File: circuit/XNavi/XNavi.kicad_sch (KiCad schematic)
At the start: 0 parts

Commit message: initial commit
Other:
- title: Template -> XNavi
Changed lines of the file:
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@@
 	(paper "A4")
 	(title_block
-		(title "Template")
+		(title "XNavi")
 		(rev "0.0")
 		(company "AIOLIA")

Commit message: 回路図&PCBを追加
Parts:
- added C10, C11, C12, C13, C14, C15, C2, C8, C9: 0.1u, Capacitor_SMD:C_0603_1608Metric_Pad1.08x0.95mm_HandSolder, symbol Device:C
- added C3: 1.0u, Capacitor_SMD:C_0603_1608Metric_Pad1.08x0.95mm_HandSolder, symbol Device:C
- added C4, C5: 2.2p, Capacitor_SMD:C_0603_1608Metric_Pad1.08x0.95mm_HandSolder, symbol Device:C
- added C6, C7: 2.2u, Capacitor_SMD:C_0603_1608Metric_Pad1.08x0.95mm_HandSolder, symbol Device:C
- added D3: LED, LED_SMD:LED_0603_1608Metric_Pad1.05x0.95mm_HandSolder, symbol Device:LED
- added D4, D5: LED, Diode_SMD:D_0603_1608Metric_Pad1.05x0.95mm_HandSolder, symbol Device:LED
- added J3: Micro_SD_Card_Det_Hirose_DM3AT, Connector_Card:microSD_HC_Hirose_DM3D-SF, symbol Connector:Micro_SD_Card_Det_Hirose_DM3AT
- added J4: Conn_01x02, Connector_JST:JST_PH_B2B-PH-SM4-TB_1x02-1MP_P2.00mm_Vertical, symbol Connector_Generic:Conn_01x02
- added J5: Conn_ST_STDC14, AIOLIA:CONN14_3220-14_CNC, symbol Connector:Conn_ST_STDC14
- added J6: Conn_01x04, Connector_JST:JST_PH_S4B-PH-SM4-TB_1x04-1MP_P2.00mm_Horizontal, symbol Connector_Generic:Conn_01x04
- added J7: Conn_02x03_Odd_Even, Connector_PinHeader_2.54mm:PinHeader_2x03_P2.54mm_Vertical, symbol Connector_Generic:Conn_02x03_Odd_Even
- added J9: Conn_Coaxial, Connector_Coaxial:U.FL_Molex_MCRF_73412-0110_Vertical, symbol Connector:Conn_Coaxial
- added JP1: Jumper_2_Open, Jumper:SolderJumper-2_P1.3mm_Open_RoundedPad1.0x1.5mm, symbol Jumper:Jumper_2_Open
- added L1: 27n, Inductor_SMD:L_0805_2012Metric_Pad1.15x1.40mm_HandSolder, symbol Device:L
- added R1, R11, R12, R2, R3, R4, R5, R6: 10k, Resistor_SMD:R_0603_1608Metric_Pad0.98x0.95mm_HandSolder, symbol Device:R
- added R10: 10k (DNP), Resistor_SMD:R_0603_1608Metric_Pad0.98x0.95mm_HandSolder, symbol Device:R
- added R13: 120, Resistor_SMD:R_0603_1608Metric_Pad0.98x0.95mm_HandSolder, symbol Device:R
- added R14: 10, Resistor_SMD:R_0603_1608Metric_Pad0.98x0.95mm_HandSolder, symbol Device:R
- added R15, R16, R17: 200, Resistor_SMD:R_0603_1608Metric_Pad0.98x0.95mm_HandSolder, symbol Device:R
- added SW1: SW_Slide, AIOLIA:SW_Slide, symbol AIOLIA:SW_Slide
- added SW2: SW_Push, Button_Switch_SMD:SW_Push_1P1T_NO_6x6mm_H9.5mm, symbol Switch:SW_Push
- added U2: ~, AIOLIA:SOT95P280X130-5N, symbol AIOLIA:NJM2866F33
- added U3: STM32H573RITx, Package_QFP:LQFP-64_10x10mm_P0.5mm, symbol MCU_ST_STM32H5:STM32H573RITx
- added U4: ~, Package_TO_SOT_SMD:SOT-23-8_Handsoldering, symbol AIOLIA:TCAN3413DDR
- added U5: ASM330LHHTR, Package_LGA:LGA-14_3x2.5mm_P0.5mm_LayoutBorder3x4y, symbol AIOLIA:ASM330LHHTR
- added U6: MAX-M10S, RF_GPS:ublox_MAX, symbol RF_GPS:MAX-M10S
- added Y1: 16MHz, Crystal:Crystal_HC52-U_Vertical, symbol Device:Crystal
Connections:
- new net: C6.1, U3.30 (VCAP)
- new net: C4.2, U3.5 (PH0), Y1.1
- new net: C5.2, U3.6 (PH1), Y1.2
- new net: C7.1, U3.62 (VCAP)
- new net: J4.1 (Pin_1), SW1.2 (B), SW1.5 (B)
- new net: D4.2 (A), R16.2
- new net: J6.2 (Pin_2), R13.1, U4.6 (CANL)
- new net: J6.1 (Pin_1), R13.2, U4.7 (CANH)
- new net: D5.2 (A), R17.2
- new net: D3.2 (A), R15.2
- new net: L1.2, R14.1
- new net: R14.2, U6.14 (VCC_RF)
- new net: J6.4 (Pin_4), JP1.1 (A)
- new net +3V3: C10.1, C11.1, C12.1, C13.1, C14.1, C15.1, C3.2, C8.1, C9.1, J3.4 (VDD), J5.3 (VCC), J7.1 (Pin_1), J7.2 (Pin_2), R1.2, R10.2, R12.1, R2.2, R3.2, R4.2, R5.2, R6.2, U2.5 (Vout), U3.1 (VBAT), U3.13 (VDDA), U3.19 (VDD), U3.32 (VDD), U3.48 (VDD), U3.64 (VDD), U4.3 (VCC), U4.5 (VIO), U5.5 (VDD_IO), U5.8 (VDD), U6.6 (V_BCKP), U6.7 (VCC_IO), U6.8 (VCC)
- new net AIN0: J7.6 (Pin_6), U3.8 (PC0)
- new net AIN1: J7.5 (Pin_5), U3.9 (PC1)
- new net AIN2: U3.10 (PC2)
- new net AIN3: U3.11 (PC3)
- new net BOOT: R10.1, R11.1, U3.60 (BOOT0)
- new net FDCAN2_RX: U3.33 (PB12), U4.4 (RXD)
- new net FDCAN2_TX: U3.34 (PB13), U4.1 (TXD)
- new net GND: C10.2, C11.2, C12.2, C13.2, C14.2, C15.2, C2.2, C3.1, C4.1, C5.1, C6.2, C7.2, C8.2, C9.2, D3.1 (K), D4.1 (K), D5.1 (K), J3.11 (SHIELD), J3.6 (VSS), J3.9 (DET_B), J4.2 (Pin_2), J5.11 (GNDDetect), J5.5 (GND), J5.7 (GND), J6.3 (Pin_3), J7.3 (Pin_3), J7.4 (Pin_4), J9.2 (Ext), R11.2, SW2.2, U2.2 (GND), U3.12 (VSSA), U3.18 (VSS), U3.31 (VSS), U3.47 (VSS), U3.63 (VSS), U4.2 (GND), U4.8 (STB), U5.2 (RES), U5.3 (RES), U5.6 (GND), U5.7 (GND), U6.1 (GND), U6.10 (GND), U6.12 (GND)
- new net I2C1_SCL: U3.58 (PB6)
- new net I2C1_SDA: U3.59 (PB7)
- new net LED0: R16.1, U3.24 (PC4)
- new net LED1: R17.1, U3.25 (PC5)
- new net LED2: U3.3 (PC14)
- new net LED3: U3.4 (PC15)
- new net PPS: R15.1, U3.41 (PA8), U6.4 (TIMEPULSE)
- new net RF: J9.1 (In), L1.1, U6.11 (RF_IN)
- new net RST: R12.2, SW2.1, U3.7 (NRST)
- new net RX1: J5.13 (VCP_RX), U3.43 (PA10)
- new net RX2: U3.17 (PA3)
- new net RX6: U3.38 (PC7), U6.3 (RXD)
- new net SDIO_CLK: J3.5 (CLK), U3.53 (PC12)
- new net SDIO_CMD: J3.3 (CMD), R3.1, U3.54 (PD2)
- new net SDIO_DAT0: J3.7 (DAT0), R4.1, U3.39 (PC8)
- new net SDIO_DAT1: J3.8 (DAT1), R5.1, U3.40 (PC9)
- new net SDIO_DAT2: J3.1 (DAT2), R1.1, U3.51 (PC10)
- new net SDIO_DAT3: J3.2 (DAT3/CD), R2.1, U3.52 (PC11)
- new net SD_DET: J3.10 (DET_A), R6.1, U3.50 (PA15(JTDI))
- new net SPI1_CS: U3.20 (PA4), U5.12 (CS)
- new net SPI1_MISO: U3.22 (PA6), U5.1 (SDO/SA0)
- new net SPI1_MOSI: U3.23 (PA7), U5.14 (SDA)
- new net SPI1_SCK: U3.21 (PA5), U5.13 (SCL)
- new net SW: U3.2 (PC13)
- new net SWCLK: J5.6 (JCLK/SWCLK), U3.49 (PA14(JTCK)
- new net SWDIO: J5.4 (JTMS/SWDIO), U3.46 (PA13(JTMS)
- new net TX1: J5.14 (VCP_TX), U3.42 (PA9)
- new net TX2: U3.16 (PA2)
- new net TX6: U3.37 (PC6), U6.2 (TXD)
- new net VCC: C2.1, JP1.2 (B), SW1.1 (A), SW1.6 (C), U2.1 (Vin), U2.3 (CONTROL)
- no-connect marks 0 -> 29
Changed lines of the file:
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@@
 	(generator "eeschema")
 	(generator_version "8.0")
-	(paper "A4")
+	(paper "A3")
 	(title_block
 		(title "XNavi")
@@
 		(company "AIOLIA")
 	)
-	(sheet_instances
-		(path "/"
-			(page "1")
-		)
-	)
-)

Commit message: MCUをRaspberry Pi Pico(2)に変更
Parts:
- removed C10, C11, C12, C13, C8, C9: 0.1u, Capacitor_SMD:C_0603_1608Metric_Pad1.08x0.95mm_HandSolder, symbol Device:C
- removed C5: 2.2p, Capacitor_SMD:C_0603_1608Metric_Pad1.08x0.95mm_HandSolder, symbol Device:C
- removed C6, C7: 2.2u, Capacitor_SMD:C_0603_1608Metric_Pad1.08x0.95mm_HandSolder, symbol Device:C
- removed J3: Micro_SD_Card_Det_Hirose_DM3AT, Connector_Card:microSD_HC_Hirose_DM3D-SF, symbol Connector:Micro_SD_Card_Det_Hirose_DM3AT
- removed J4: Conn_01x02, Connector_JST:JST_PH_B2B-PH-SM4-TB_1x02-1MP_P2.00mm_Vertical, symbol Connector_Generic:Conn_01x02
- removed J5: Conn_ST_STDC14, AIOLIA:CONN14_3220-14_CNC, symbol Connector:Conn_ST_STDC14
- removed J6: Conn_01x04, Connector_JST:JST_PH_S4B-PH-SM4-TB_1x04-1MP_P2.00mm_Horizontal, symbol Connector_Generic:Conn_01x04
- removed J7: Conn_02x03_Odd_Even, Connector_PinHeader_2.54mm:PinHeader_2x03_P2.54mm_Vertical, symbol Connector_Generic:Conn_02x03_Odd_Even
- removed JP1: Jumper_2_Open, Jumper:SolderJumper-2_P1.3mm_Open_RoundedPad1.0x1.5mm, symbol Jumper:Jumper_2_Open
- removed R10: 10k (DNP), Resistor_SMD:R_0603_1608Metric_Pad0.98x0.95mm_HandSolder, symbol Device:R
- removed R11, R12, R4, R5, R6: 10k, Resistor_SMD:R_0603_1608Metric_Pad0.98x0.95mm_HandSolder, symbol Device:R
- removed R13: 120, Resistor_SMD:R_0603_1608Metric_Pad0.98x0.95mm_HandSolder, symbol Device:R
- removed SW1: SW_Slide, AIOLIA:SW_Slide, symbol AIOLIA:SW_Slide
- removed SW2: SW_Push, Button_Switch_SMD:SW_Push_1P1T_NO_6x6mm_H9.5mm, symbol Switch:SW_Push
- removed U2: ~, AIOLIA:SOT95P280X130-5N, symbol AIOLIA:NJM2866F33
- removed U3: STM32H573RITx, Package_QFP:LQFP-64_10x10mm_P0.5mm, symbol MCU_ST_STM32H5:STM32H573RITx
- removed U4: ~, Package_TO_SOT_SMD:SOT-23-8_Handsoldering, symbol AIOLIA:TCAN3413DDR
- removed Y1: 16MHz, Crystal:Crystal_HC52-U_Vertical, symbol Device:Crystal
- added A1: RaspberryPi_Pico, Module:RaspberryPi_Pico_SMD_HandSolder, symbol MCU_Module:RaspberryPi_Pico_Debug
- added C1: 0.1u, Capacitor_SMD:C_0603_1608Metric_Pad1.08x0.95mm_HandSolder, symbol Device:C
- added D4: LED, Diode_SMD:D_0603_1608Metric_Pad1.05x0.95mm_HandSolder, symbol Device:LED
- added J1: Micro_SD_Card_Det, Connector_Card:microSD_HC_Hirose_DM3AT-SF-PEJM5, symbol Connector:Micro_SD_Card_Det
- added J2, J4: Conn_01x06, Connector_JST:JST_ZH_B6B-ZR_1x06_P1.50mm_Vertical, symbol Connector_Generic:Conn_01x06
- added J3: Conn_01x04, Connector_JST:JST_PH_S4B-PH-K_1x04_P2.00mm_Horizontal, symbol Connector_Generic:Conn_01x04
- added J5: Conn_01x02, Connector_JST:JST_PH_S2B-PH-SM4-TB_1x02-1MP_P2.00mm_Horizontal, symbol Connector_Generic:Conn_01x02
- added R8: 200, Resistor_SMD:R_0603_1608Metric_Pad0.98x0.95mm_HandSolder, symbol Device:R
- added U1: STM32G441KBTx, Package_QFP:LQFP-32_7x7mm_P0.8mm, symbol MCU_ST_STM32G4:STM32G441KBTx
- added U2: ~, Package_TO_SOT_SMD:SOT-23-8_Handsoldering, symbol AIOLIA:TCAN3413DDR
- C3: value 1.0u -> 0.1u
- C4: value 2.2p -> 0.1u
- R1, R2: value 10k -> 100
- R3: value 10k -> 120
- renumbered C14 to C5, C15 to C6, D3 to D1, D4 to D2, D5 to D3, J9 to J6, R14 to R4, R15 to R5, R16 to R6, R17 to R7, U5 to U3, U6 to U4
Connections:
- net RX6 is gone; now on net RX1: U4.3 (RXD)
- net SDIO_DAT3 is gone; now on net GND: R2.1
- net TX6 is gone; now on net TX1: U4.2 (TXD)
- net +3V3: now also C2.1, C3.1, C4.2, A1.36 (3V3), C1.1, J1.4 (VDD), U1.1 (VDD), U1.15 (VDDA), U1.17 (VDD), U2.3 (VCC), U2.5 (VIO); no longer C3.2, R2.2, R3.2
- net GND: now also C3.2, A1.13 (GND), A1.18 (GND), A1.23 (GND), A1.28 (GND), A1.3 (GND), A1.33 (AGND), A1.38 (GND), A1.8 (GND), A1.D2 (GND), C1.2, D4.1 (K), J1.11 (SHIELD), J1.6 (VSS), J2.6 (Pin_6), J3.2 (Pin_2), J4.6 (Pin_6), J5.2 (Pin_2), U1.14 (VSSA), U1.16 (VSS), U1.32 (VSS), U2.2 (GND), U2.8 (STB); no longer C3.1
- net LED0: now also A1.14 (GPIO10)
- net LED1: now also A1.15 (GPIO11)
- net LED2: now also R8.1, U1.18 (PA8)
- net PPS: now also A1.4 (GPIO2)
- net RST: now also U1.4 (PG10)
- net RX1: now also A1.2 (GPIO1)
- net RX2: now also A1.12 (GPIO9), U1.7 (PA2)
- net SPI1_CS: now also A1.17 (GPIO13)
- net SPI1_MISO: now also A1.16 (GPIO12)
- net SPI1_MOSI: now also A1.20 (GPIO15)
- net SPI1_SCK: now also A1.19 (GPIO14)
- net SWCLK: now also A1.D1 (SWCLK), J4.4 (Pin_4)
- net SWDIO: now also A1.D3 (SWDIO), J4.3 (Pin_3)
- net TX1: now also A1.1 (GPIO0)
- net TX2: now also A1.11 (GPIO8), U1.8 (PA3)
- net VCC: now also A1.39 (VSYS), J3.1 (Pin_1), J5.1 (Pin_1); no longer C2.1
- net SDIO_CMD renamed CAN-
- net CAN-: now also J3.3 (Pin_3), U2.6 (CANL)
- net SDIO_DAT2 renamed BOOT0
- net BOOT0: now also R2.2, U1.31 (PB8)
- new net: D4.2 (A), R8.2
- new net CAN+: J3.4 (Pin_4), R3.2, U2.7 (CANH)
- new net CAN_RX: U1.21 (PA11), U2.4 (RXD)
- new net CAN_TX: U1.22 (PA12), U2.1 (TXD)
- new net SPI-CS: A1.22 (GPIO17), J1.2 (DAT3/CD)
- new net SPI-MISO: A1.21 (GPIO16), J1.7 (DAT0)
- new net SPI-MOSI: A1.25 (GPIO19), J1.3 (CMD)
- new net SPI-SCK: A1.24 (GPIO18), J1.5 (CLK)
- new net SWCLK_STM32: J2.4 (Pin_4), U1.24 (PA14)
- new net SWDIO_STM32: J2.3 (Pin_3), U1.23 (PA13)
- no-connect marks 29 -> 51
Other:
- note added: "micro SD"

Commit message: RS485追加 & シルク追加
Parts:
- added J7: Conn_01x04, Connector_JST:JST_PH_S4B-PH-SM4-TB_1x04-1MP_P2.00mm_Horizontal, symbol Connector_Generic:Conn_01x04
- added R9: 120, Resistor_SMD:R_0603_1608Metric_Pad0.98x0.95mm_HandSolder, symbol Device:R
- added U5: MAX3485, Package_SO:SOP-8_3.76x4.96mm_P1.27mm, symbol Interface_UART:MAX3485
- D1: footprint LED_SMD:LED_0603_1608Metric_Pad1.05x0.95mm_HandSolder -> Diode_SMD:D_0603_1608Metric_Pad1.05x0.95mm_HandSolder
- J3: footprint Connector_JST:JST_PH_S4B-PH-K_1x04_P2.00mm_Horizontal -> Connector_JST:JST_PH_S4B-PH-SM4-TB_1x04-1MP_P2.00mm_Horizontal
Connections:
- net +3V3: now also U5.8 (VCC)
- net GND: now also J7.3 (Pin_3), U5.2 (~{RE}), U5.3 (DE), U5.5 (GND)
- net TX1_STM32: now reaches U1.19 (PA9)
- net TX1_STM32: now also U5.4 (DI)
- net RX1_STM32: now reaches U1.20 (PA10)
- net RX1_STM32: now also U5.1 (RO)
- new net: J7.1 (Pin_1), R9.1, U5.7 (B)
- new net: J7.2 (Pin_2), R9.2, U5.6 (A)
- no-connect marks 51 -> 50

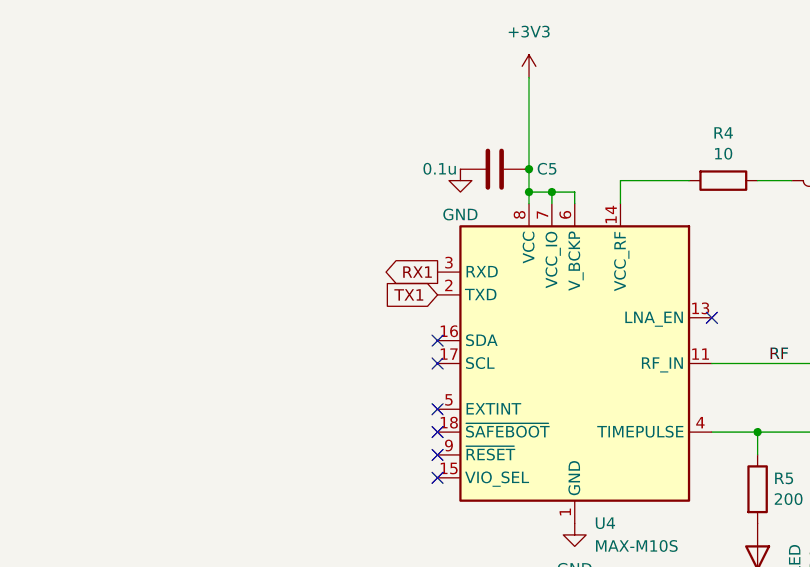
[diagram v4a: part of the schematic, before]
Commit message: UARTの信号線変更,基板を発注
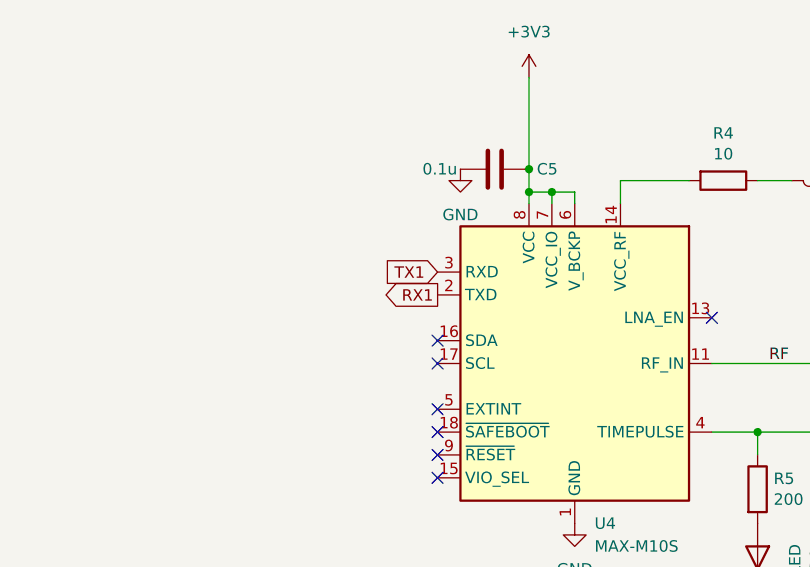
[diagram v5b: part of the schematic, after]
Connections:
- net RX1: now also U4.2 (TXD); no longer U4.3 (RXD)
- net TX1: now also U4.3 (RXD); no longer U4.2 (TXD)
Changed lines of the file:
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@@
 		)
 	)
-	(global_label "TX1"
-		(shape input)
+	(global_label "CAN_RX"
+		(shape input)
+		(at 63.5 226.06 0)
+		(fields_autoplaced yes)
+		(effects
+			(font
+				(size 1.27 1.27)
+			)
+			(justify left)
+		)
+		(property "Intersheetrefs" "${INTERSHEET_REFS}"
+			(at 73.6214 226.06 0)
+			(effects
+				(font
+					(size 1.27 1.27)
+				)
+				(justify left)
+				(hide yes)
+			)
+		)
+	)
+	(global_label "CAN_TX"
+		(shape output)
+		(at 63.5 228.6 0)
+		(fields_autoplaced yes)
+		(effects
+			(font
+				(size 1.27 1.27)
+			)
+			(justify left)
+		)
+		(property "Intersheetrefs" "${INTERSHEET_REFS}"
+			(at 73.319 228.6 0)
+			(effects
+				(font
+					(size 1.27 1.27)
+				)
+				(justify left)
+				(hide yes)
+			)
+		)
+	)
+	(global_label "SPI1_MOSI"
+		(shape input)
+		(at 377.19 149.86 0)
+		(fields_autoplaced yes)
+		(effects
+			(font
+				(size 1.27 1.27)
+			)
+			(justify left)
+		)
+		(property "Intersheetrefs" "${INTERSHEET_REFS}"
+			(at 390.0328 149.86 0)
+			(effects
+				(font
+					(size 1.27 1.27)
+				)
+				(justify left)
+				(hide yes)
+			)
+		)
+	)
+	(global_label "SPI1_CS"
+		(shape input)
+		(at 377.19 154.94 0)
+		(fields_autoplaced yes)
+		(effects
+			(font
+				(size 1.27 1.27)
+			)
+			(justify left)
+		)
+		(property "Intersheetrefs" "${INTERSHEET_REFS}"
+			(at 387.9161 154.94 0)
+			(effects
+				(font
+					(size 1.27 1.27)
+				)
+				(justify left)
+				(hide yes)
+			)
+		)
+	)
+	(global_label "RX1"
+		(shape output)
 		(at 334.01 83.82 180)
 		(fields_autoplaced yes)
@@
 		)
 		(property "Intersheetrefs" "${INTERSHEET_REFS}"
-			(at 327.6382 83.82 0)
-			(effects
-				(font
-					(size 1.27 1.27)
-				)
-				(justify right)
-				(hide yes)
-			)
-		)
-	)
-	(global_label "CAN_RX"
-		(shape input)
-		(at 63.5 226.06 0)
-		(fields_autoplaced yes)
-		(effects
-			(font
-				(size 1.27 1.27)
-			)
-			(justify left)
-		)
-		(property "Intersheetrefs" "${INTERSHEET_REFS}"
-			(at 73.6214 226.06 0)
-			(effects
-				(font
-					(size 1.27 1.27)
-				)
-				(justify left)
-				(hide yes)
-			)
-		)
-	)
-	(global_label "CAN_TX"
-		(shape output)
-		(at 63.5 228.6 0)
-		(fields_autoplaced yes)
-		(effects
-			(font
-				(size 1.27 1.27)
-			)
-			(justify left)
-		)
-		(property "Intersheetrefs" "${INTERSHEET_REFS}"
-			(at 73.319 228.6 0)
-			(effects
-				(font
-					(size 1.27 1.27)
-				)
-				(justify left)
-				(hide yes)
-			)
-		)
-	)
-	(global_label "SPI1_MOSI"
-		(shape input)
-		(at 377.19 149.86 0)
-		(fields_autoplaced yes)
-		(effects
-			(font
-				(size 1.27 1.27)
-			)
-			(justify left)
-		)
-		(property "Intersheetrefs" "${INTERSHEET_REFS}"
-			(at 390.0328 149.86 0)
-			(effects
-				(font
-					(size 1.27 1.27)
-				)
-				(justify left)
-				(hide yes)
-			)
-		)
-	)
-	(global_label "SPI1_CS"
-		(shape input)
-		(at 377.19 154.94 0)
-		(fields_autoplaced yes)
-		(effects
-			(font
-				(size 1.27 1.27)
-			)
-			(justify left)
-		)
-		(property "Intersheetrefs" "${INTERSHEET_REFS}"
-			(at 387.9161 154.94 0)
-			(effects
-				(font
-					(size 1.27 1.27)
-				)
-				(justify left)
-				(hide yes)
-			)
-		)
-	)
-	(global_label "RX1"
-		(shape output)
-		(at 334.01 81.28 180)
-		(fields_autoplaced yes)
-		(effects
-			(font
-				(size 1.27 1.27)
-			)
-			(justify right)
-		)
-		(property "Intersheetrefs" "${INTERSHEET_REFS}"
-			(at 327.3358 81.28 0)
+			(at 327.3358 83.82 0)
 			(effects
 				(font
@@
 				(hide yes)
 			)
+		)
+	)
+	(global_label "TX1"
+		(shape input)
+		(at 334.01 81.28 180)
+		(fields_autoplaced yes)
+		(effects
+			(font
+				(size 1.27 1.27)
+			)
+			(justify right)
+		)
+		(property "Intersheetrefs" "${INTERSHEET_REFS}"
+			(at 327.6382 81.28 0)
+			(effects
+				(font
+					(size 1.27 1.27)
+				)
+				(justify right)
+				(hide yes)
+			)
